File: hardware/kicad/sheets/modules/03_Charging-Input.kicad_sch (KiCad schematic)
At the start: 0 parts

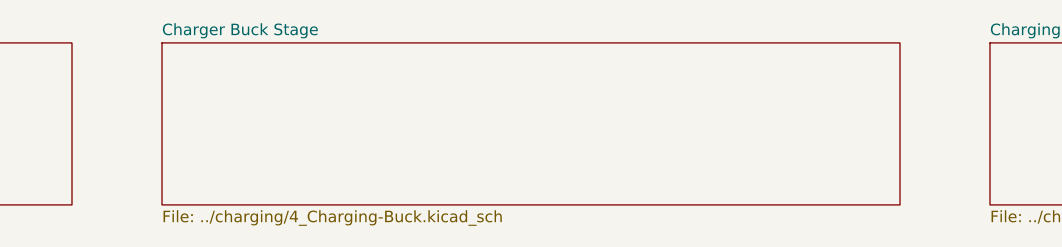
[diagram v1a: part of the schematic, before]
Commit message: clearer power path with sheets
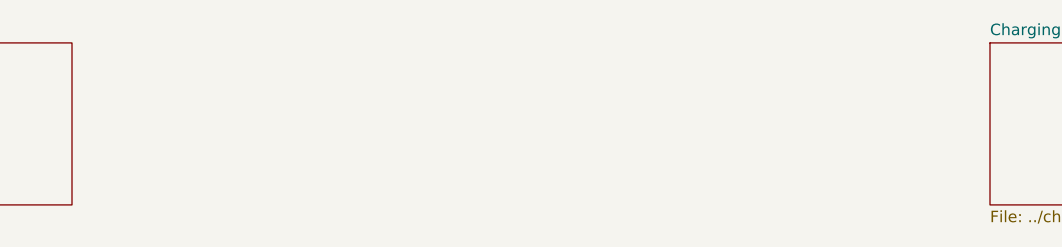
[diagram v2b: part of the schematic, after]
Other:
- removed sheet Charger Buck Stage
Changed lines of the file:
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@@
-	)
-	(sheet
-		(at 102 15)
-		(size 82 18)
-		(exclude_from_sim no)
-		(in_bom yes)
-		(on_board yes)
-		(dnp no)
-		(fields_autoplaced yes)
-		(stroke
-			(width 0)
-			(type solid)
-		)
-		(fill
-			(color 0 0 0 0.0000)
-		)
-		(property "Sheetname" "Charger Buck Stage"
-			(at 102 14.2884 0)
-			(effects
-				(font
-					(size 1.27 1.27)
-				)
-				(justify left bottom)
-			)
-		)
-		(property "Sheetfile" "../charging/4_Charging-Buck.kicad_sch"
-			(at 102 33.5846 0)
-			(effects
-				(font
-					(size 1.27 1.27)
-				)
-				(justify left top)
-			)
-		)
 	)
 	(sheet

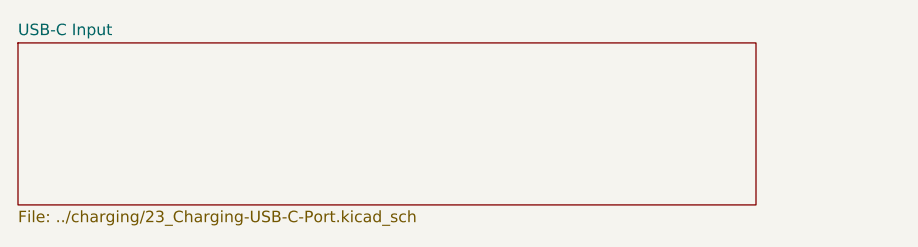
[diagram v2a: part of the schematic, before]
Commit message: resheeted bms and fixed links for the 12v buck
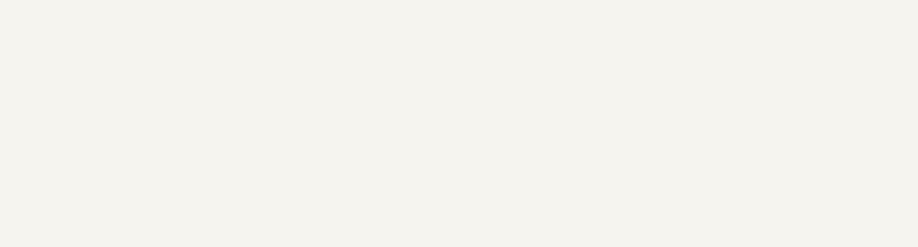
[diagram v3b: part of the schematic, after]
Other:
- removed sheet USB-C Input
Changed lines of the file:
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@@
-	)
-	(sheet
-		(at 10 15)
-		(size 82 18)
-		(exclude_from_sim no)
-		(in_bom yes)
-		(on_board yes)
-		(dnp no)
-		(fields_autoplaced yes)
-		(stroke
-			(width 0)
-			(type solid)
-		)
-		(fill
-			(color 0 0 0 0.0000)
-		)
-		(property "Sheetname" "USB-C Input"
-			(at 10 14.2884 0)
-			(effects
-				(font
-					(size 1.27 1.27)
-				)
-				(justify left bottom)
-			)
-		)
-		(property "Sheetfile" "../charging/23_Charging-USB-C-Port.kicad_sch"
-			(at 10 33.5846 0)
-			(effects
-				(font
-					(size 1.27 1.27)
-				)
-				(justify left top)
-			)
-		)
 	)
 	(sheet
